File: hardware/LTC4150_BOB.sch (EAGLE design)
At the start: 23 parts, among them U1 LTC4150

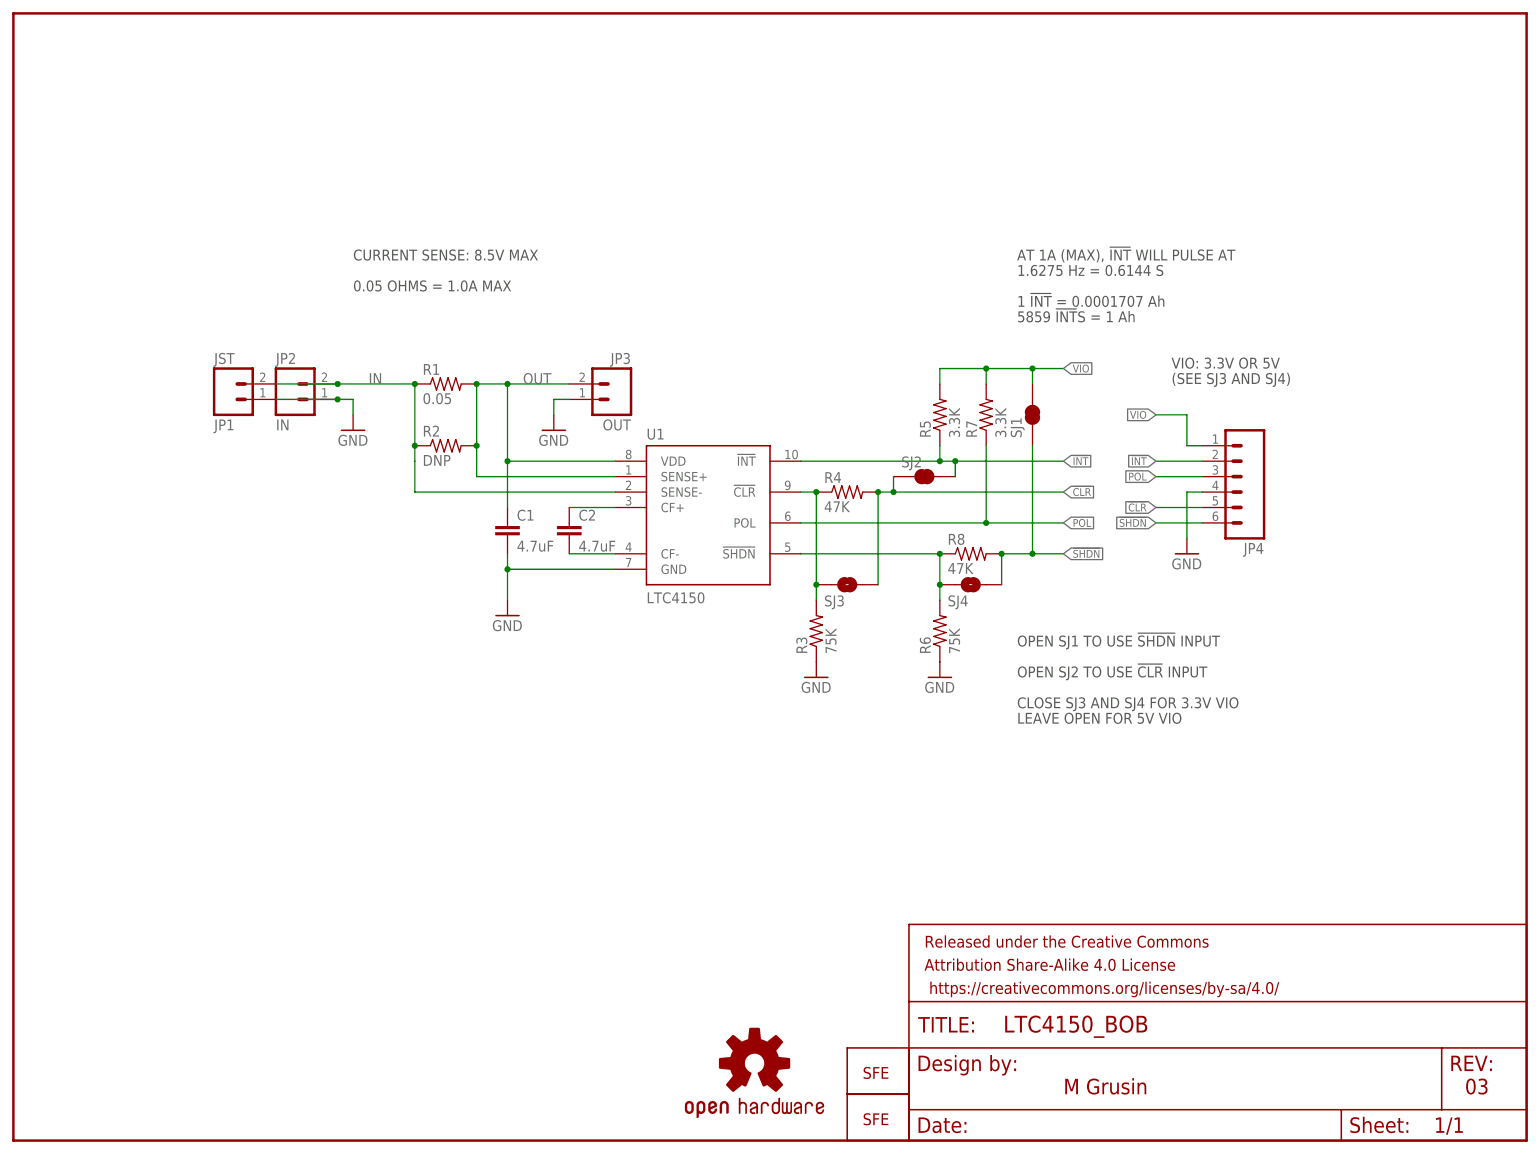
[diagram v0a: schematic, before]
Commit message: Rename and rearrange repository
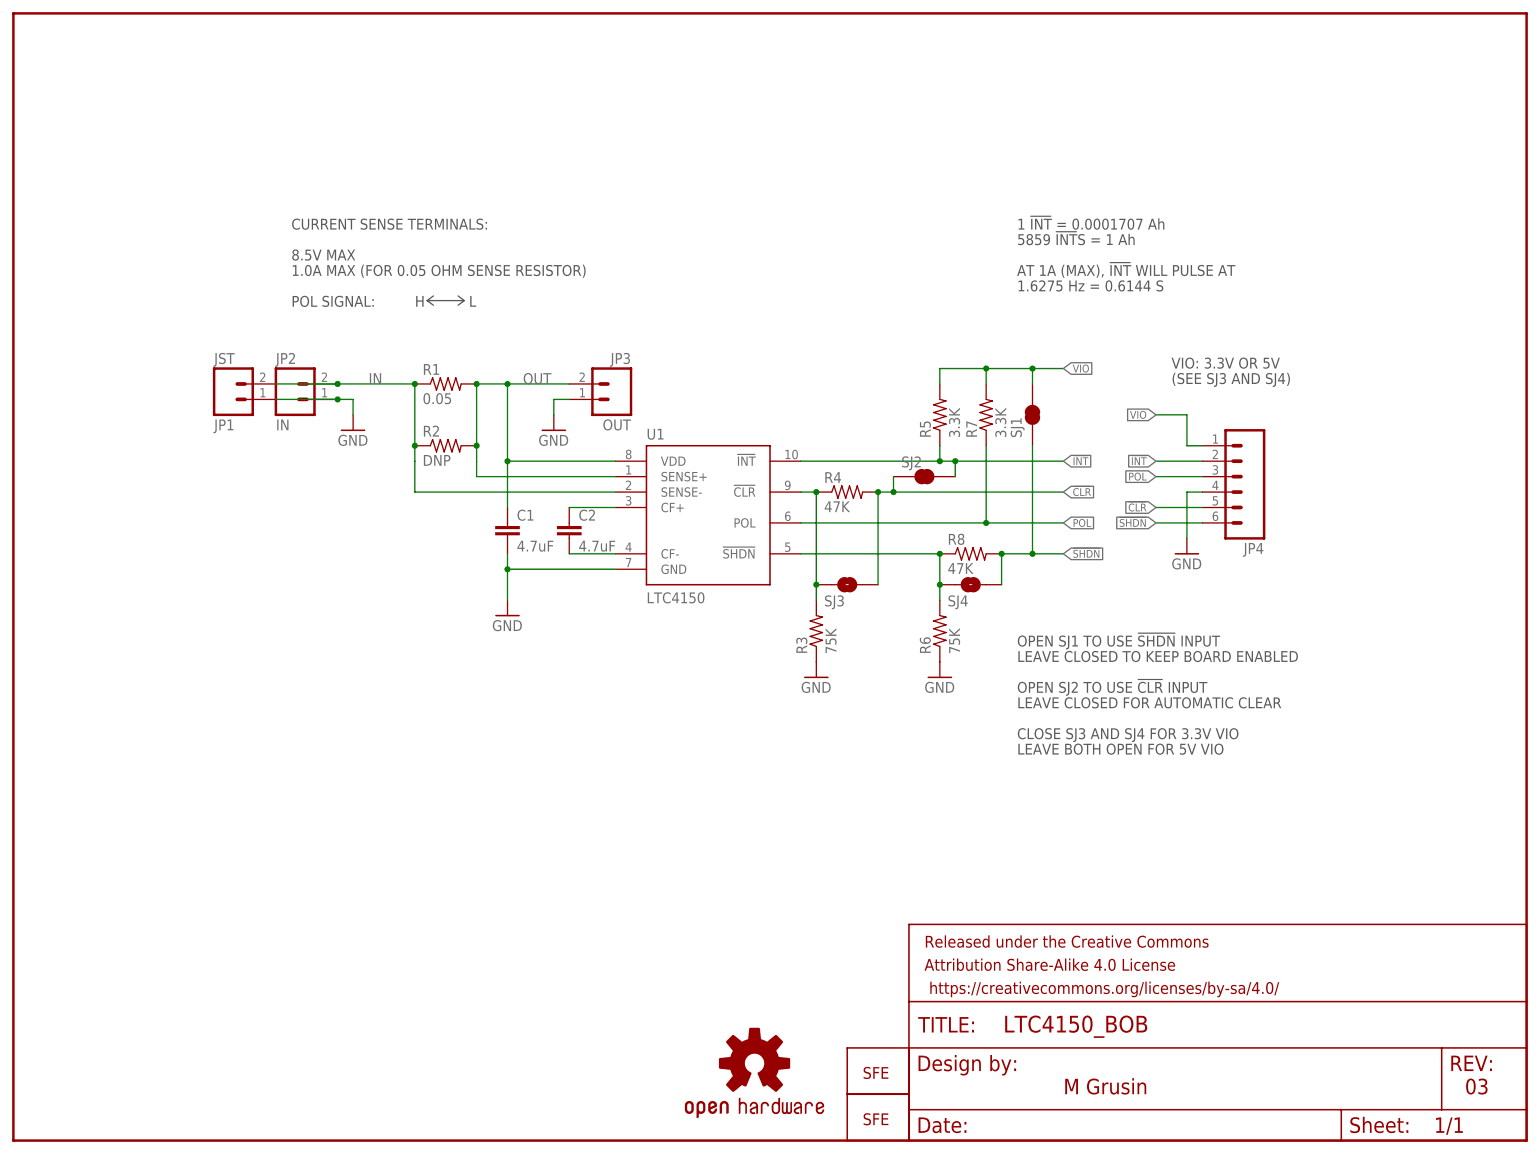
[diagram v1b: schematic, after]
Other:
- note added: "1.0A MAX (FOR 0.05 OHM SENSE RESISTOR)"
- note added: "8.5V MAX"
- note added: "CURRENT SENSE TERMINALS:"
- note added: "H"
- note added: "L"
- note added: "LEAVE BOTH OPEN FOR 5V VIO"
- note added: "LEAVE CLOSED FOR AUTOMATIC CLEAR"
- note added: "LEAVE CLOSED TO KEEP BOARD ENABLED"
- note added: "POL SIGNAL:"
- note removed: "0.05 OHMS = 1.0A MAX"
- note removed: "CURRENT SENSE: 8.5V MAX"
- note removed: "LEAVE OPEN FOR 5V VIO"
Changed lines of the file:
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@@
 <text x="172.72" y="7.62" size="2.54" layer="94">M Grusin</text>
 <text x="238.76" y="7.62" size="2.54" layer="94">03</text>
-<text x="165.1" y="71.12" size="1.778" layer="97">CLOSE SJ3 AND SJ4 FOR 3.3V VIO</text>
+<text x="165.1" y="66.04" size="1.778" layer="97">CLOSE SJ3 AND SJ4 FOR 3.3V VIO</text>
 <text x="165.1" y="81.28" size="1.778" layer="97">OPEN SJ1 TO USE !SHDN! INPUT</text>
-<text x="55.88" y="144.78" size="1.778" layer="97">CURRENT SENSE: 8.5V MAX</text>
-<text x="165.1" y="68.58" size="1.778" layer="97">LEAVE OPEN FOR 5V VIO</text>
-<text x="165.1" y="144.78" size="1.778" layer="97">AT 1A (MAX), !INT! WILL PULSE AT</text>
-<text x="165.1" y="142.24" size="1.778" layer="97">1.6275 Hz = 0.6144 S</text>
-<text x="165.1" y="137.16" size="1.778" layer="97">1 !INT! = 0.0001707 Ah</text>
-<text x="165.1" y="134.62" size="1.778" layer="97">5859 !INT!S = 1 Ah</text>
-<text x="165.1" y="76.2" size="1.778" layer="97">OPEN SJ2 TO USE !CLR! INPUT</text>
+<text x="45.72" y="149.86" size="1.778" layer="97">CURRENT SENSE TERMINALS:</text>
+<text x="165.1" y="63.5" size="1.778" layer="97">LEAVE BOTH OPEN FOR 5V VIO</text>
+<text x="165.1" y="142.24" size="1.778" layer="97">AT 1A (MAX), !INT! WILL PULSE AT</text>
+<text x="165.1" y="139.7" size="1.778" layer="97">1.6275 Hz = 0.6144 S</text>
+<text x="165.1" y="149.86" size="1.778" layer="97">1 !INT! = 0.0001707 Ah</text>
+<text x="165.1" y="147.32" size="1.778" layer="97">5859 !INT!S = 1 Ah</text>
+<text x="165.1" y="73.66" size="1.778" layer="97">OPEN SJ2 TO USE !CLR! INPUT</text>
 <rectangle x1="149.098" y1="108.712" x2="150.622" y2="109.728" layer="94"/>
 <rectangle x1="167.132" y1="118.364" x2="168.148" y2="120.142" layer="94"/>
-<text x="55.88" y="139.7" size="1.778" layer="97">0.05 OHMS = 1.0A MAX</text>
+<text x="45.72" y="142.24" size="1.778" layer="97">1.0A MAX (FOR 0.05 OHM SENSE RESISTOR)</text>
 <text x="190.5" y="127" size="1.778" layer="97">VIO: 3.3V OR 5V</text>
 <text x="190.5" y="124.46" size="1.778" layer="97">(SEE SJ3 AND SJ4)</text>
+<text x="165.1" y="78.74" size="1.778" layer="97">LEAVE CLOSED TO KEEP BOARD ENABLED</text>
+<text x="165.1" y="71.12" size="1.778" layer="97">LEAVE CLOSED FOR AUTOMATIC CLEAR</text>
+<text x="45.72" y="144.78" size="1.778" layer="97">8.5V MAX</text>
+<text x="45.72" y="137.16" size="1.778" layer="97">POL SIGNAL:</text>
+<text x="66.04" y="137.16" size="1.778" layer="97">H</text>
+<text x="74.93" y="137.16" size="1.778" layer="97">L</text>
+<wire x1="68.072" y1="138.176" x2="69.088" y2="138.938" width="0.1524" layer="97"/>
+<wire x1="68.072" y1="138.176" x2="69.088" y2="137.414" width="0.1524" layer="97"/>
+<wire x1="73.152" y1="138.938" x2="74.168" y2="138.176" width="0.1524" layer="97"/>
+<wire x1="74.168" y1="138.176" x2="73.152" y2="137.414" width="0.1524" layer="97"/>
+<wire x1="74.168" y1="138.176" x2="68.072" y2="138.176" width="0.1524" layer="97"/>
 </plain>
 <instances>

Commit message: Changed version to 1.0 for reds
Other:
- note added: "10"
- note removed: "03"
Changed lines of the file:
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@@
 <plain>
 <text x="172.72" y="7.62" size="2.54" layer="94">M Grusin</text>
-<text x="238.76" y="7.62" size="2.54" layer="94">03</text>
+<text x="238.76" y="7.62" size="2.54" layer="94">10</text>
 <text x="165.1" y="66.04" size="1.778" layer="97">CLOSE SJ3 AND SJ4 FOR 3.3V VIO</text>
 <text x="165.1" y="81.28" size="1.778" layer="97">OPEN SJ1 TO USE !SHDN! INPUT</text>
